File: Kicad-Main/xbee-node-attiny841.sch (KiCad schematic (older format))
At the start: 40 parts, among them P10 CONN_1, P11 CONN_1, P12 CONN_1, P13 CONN_1, P14 CONN_1, P15 CONN_1, P16 CONN_1, P17 CONN_1, P18 CONN_1, P2 XBee Adaptor, P3 Test, P4 Battery, P5 XBee-ext-1, P6 XBee-ext-2, P7 CONN_1, P8 CONN_1, P9 CONN_1, Q2 S9014, Q3 2N7000, U1 ATTINY841, U2 MAX952ESA, U3 TPS77033

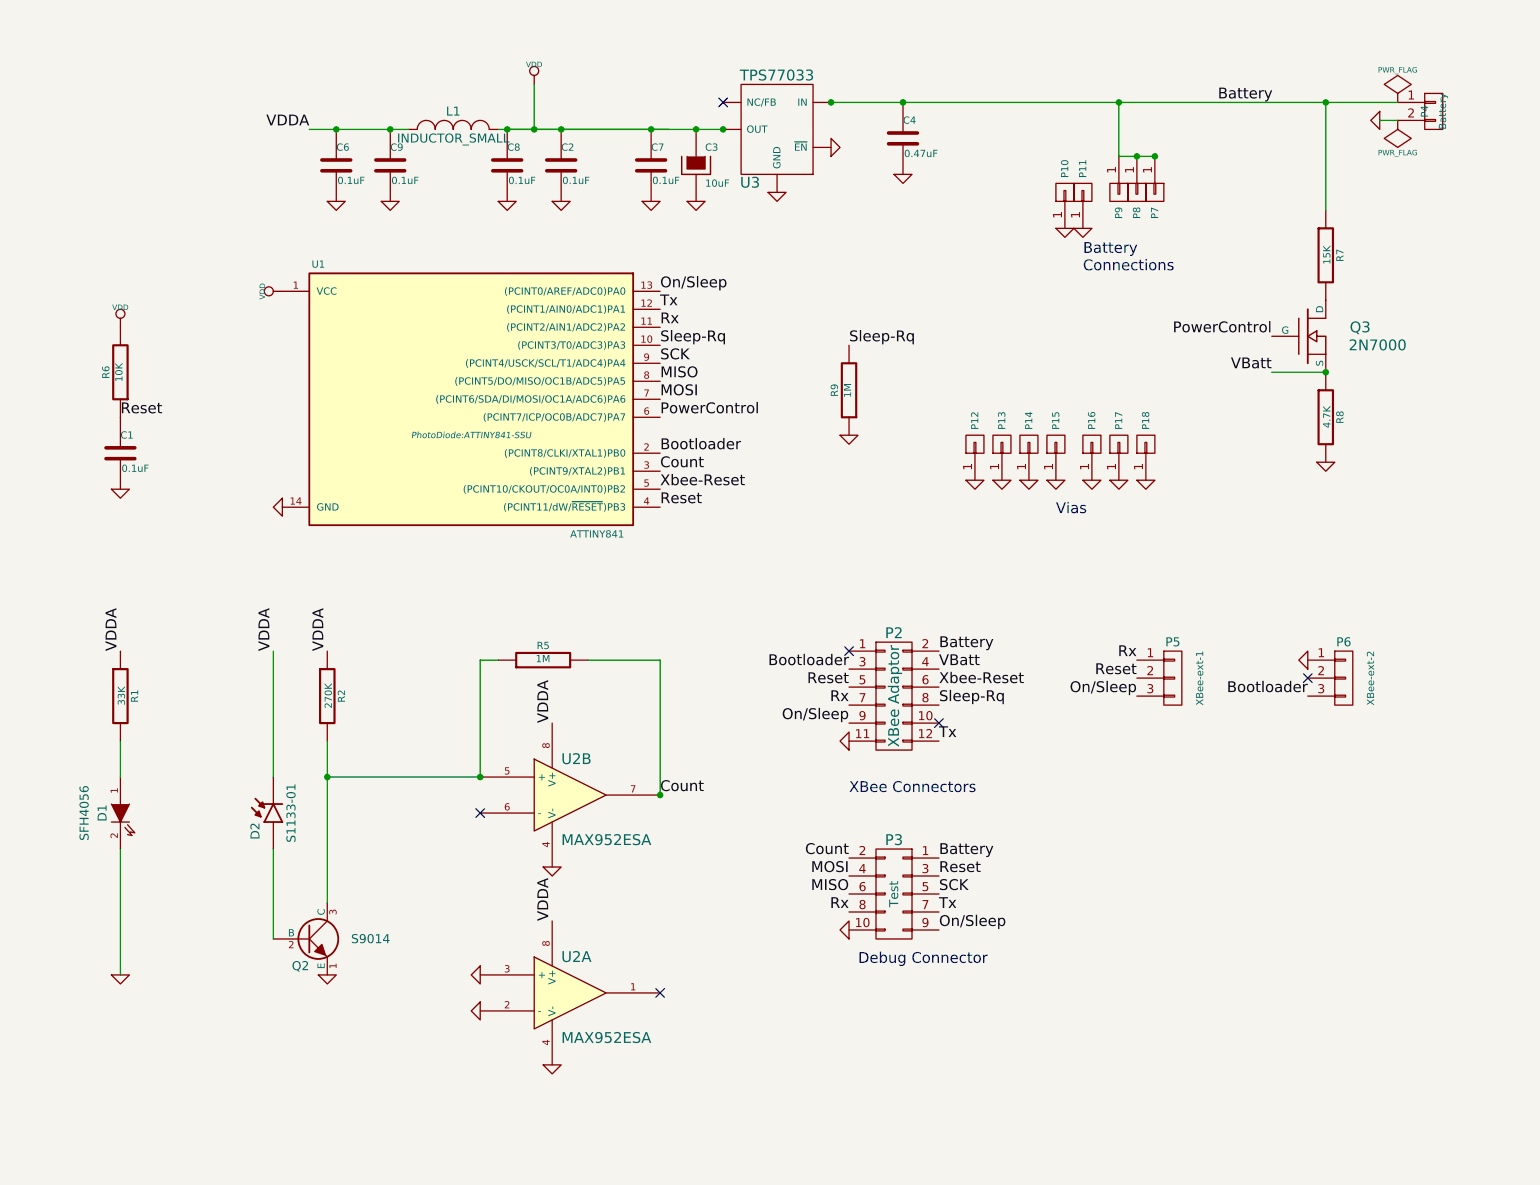
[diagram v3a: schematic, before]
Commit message: Major new version of the PCBs for next stage of production run.
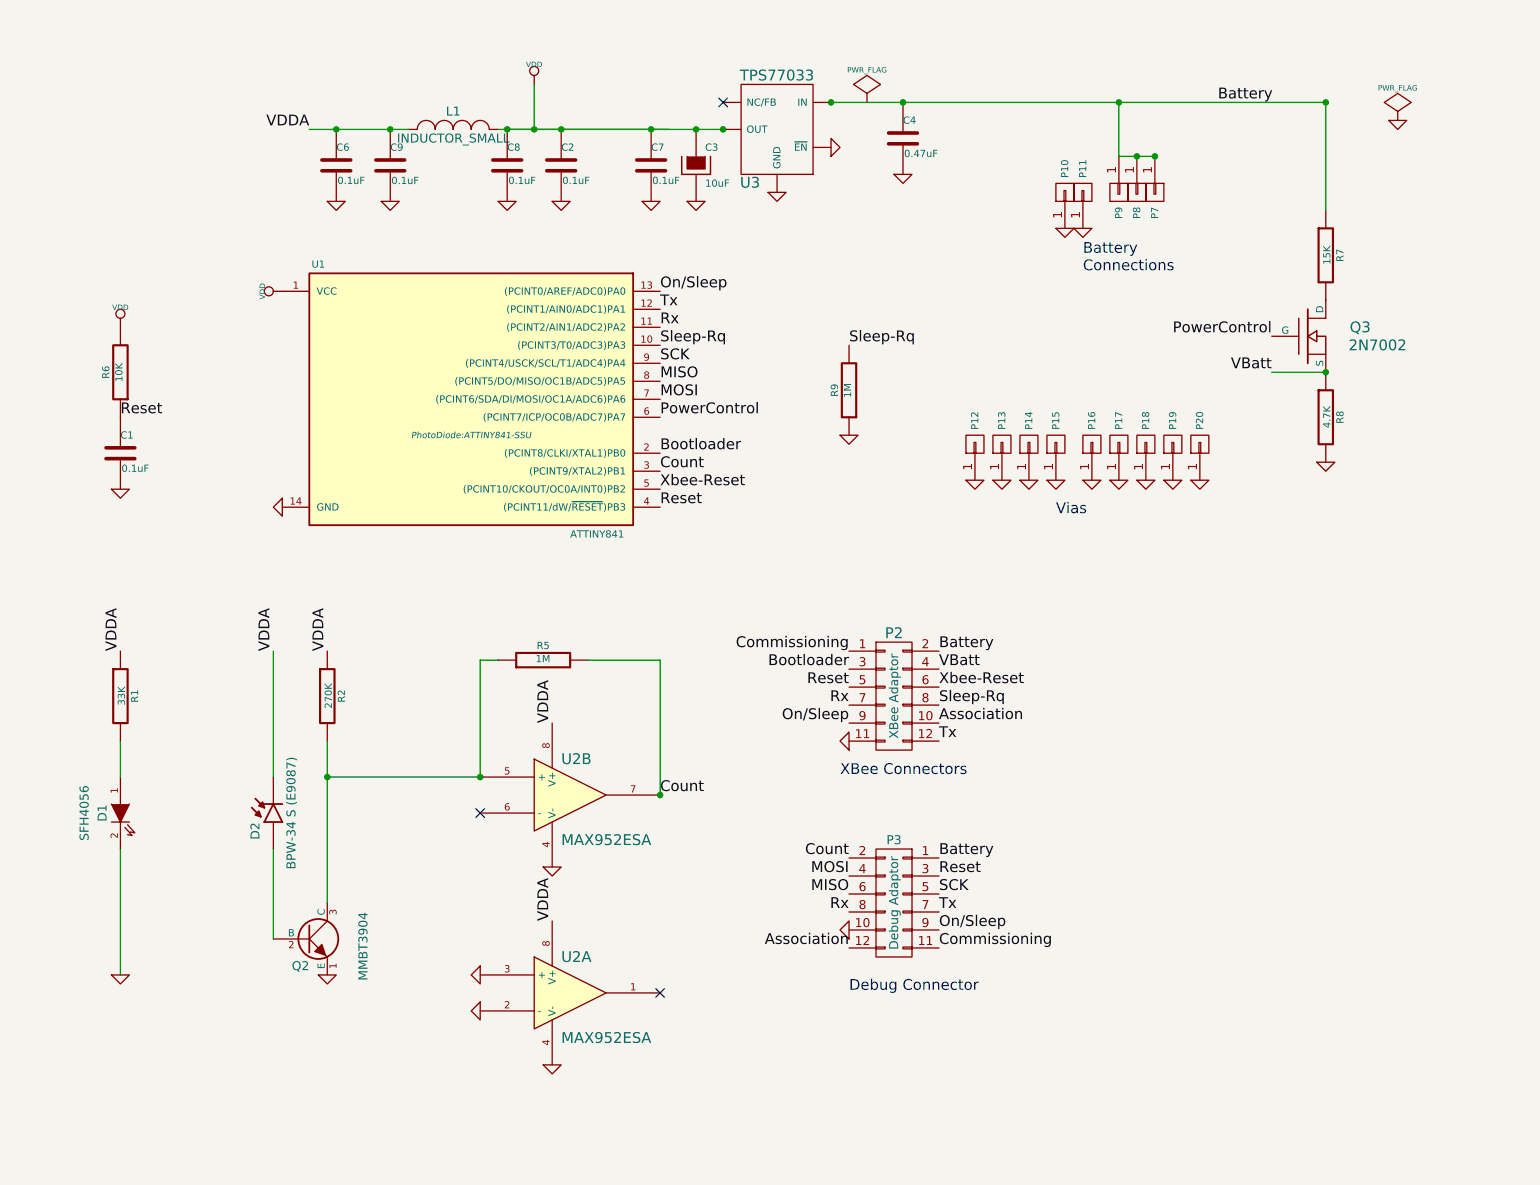
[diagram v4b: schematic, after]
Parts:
- removed P3: Test, PhotoDiode:pin_header_2mm_2x5, symbol CONN_02X05
- removed P4: Battery, PhotoDiode:SIL-2, symbol CONN_01X02
- removed P5: XBee-ext-1, PhotoDiode:pin_header_2mm_1x3, symbol CONN_01X03
- removed P6: XBee-ext-2, PhotoDiode:pin_header_2mm_1x3, symbol CONN_01X03
- added P19, P20: CONN_1, PhotoDiode:THROUGHVIA, symbol CONN_01X01
- added P3: Debug Adaptor, PhotoDiode:pin_smd_header_2mm_2x6, symbol CONN_02X06
- D2: value S1133-01 -> BPW-34 S (E9087); footprint PhotoDiode:S1133TH -> PhotoDiode:BPW34
- L1: footprint PhotoDiode:SM0603_Resistor -> PhotoDiode:R_0805
- Q2: value S9014 -> MMBT3904
- Q3: value 2N7000 -> 2N7002
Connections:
- net labels added: Association, Commissioning
- wire segments 20 -> 19
- no-connect marks 6 -> 3
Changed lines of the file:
@@
 Sheet 1 1
 Title "XBee ATTiny4313 Counting Node"
-Date "26 Jul 2014"
-Rev "0.0"
+Date "08 April 2016"
+Rev "1.0"
 Comp "K. Sarkies"
 Comment1 ""
@@
 $EndDescr
 $Comp
-L CONN_01X02 P4
-U 1 1 53D32A7E
-P 10250 1450
-F 0 "P4" V 10200 1450 40  0000 C CNN
-F 1 "Battery" V 10300 1450 40  0000 C CNN
-F 2 "PhotoDiode:SIL-2" H 10250 1450 60  0001 C CNN
-F 3 "" H 10250 1450 60  0000 C CNN
-	1    10250 1450
-	1    0    0    -1
-$EndComp
-$Comp
 L MOSFET_N-RESCUE-xbee-node-attiny841 Q3
 U 1 1 53D32AE5
 P 9550 2700
 F 0 "Q3" H 9900 2750 60  0000 R CNN
-F 1 "2N7000" H 10100 2650 60  0000 R CNN
+F 1 "2N7002" H 10100 2650 60  0000 R CNN
 F 2 "PhotoDiode:SOT23GDS" H 9550 2700 60  0001 C CNN
 F 3 "" H 9550 2700 60  0000 C CNN
@@
 P 4000 6050
 F 0 "Q2" H 4000 5900 50  0000 R CNN
-F 1 "S9014" H 4450 6050 50  0000 R CNN
+F 1 "MMBT3904" V 4300 6200 50  0000 R CNN
 F 2 "PhotoDiode:SOT23EBC" H 4000 6050 60  0001 C CNN
 F 3 "" H 4000 6050 60  0000 C CNN
@@
 P 7250 4700
 F 0 "P2" H 7250 5050 60  0000 C CNN
-F 1 "XBee Adaptor" V 7250 4700 60  0000 C CNN
+F 1 "XBee Adaptor" V 7250 4700 50  0000 C CNN
 F 2 "PhotoDiode:pin_header_2mm_2x6" H 7250 4700 60  0001 C CNN
 F 3 "" H 7250 4700 60  0000 C CNN
@@
 	1    2950 3350
 	1    0    0    -1
-$EndComp
-$Comp
-L CONN_02X05 P3
-U 1 1 53E0177A
-P 7250 5800
-F 0 "P3" H 7250 6100 60  0000 C CNN
-F 1 "Test" V 7250 5800 50  0000 C CNN
-F 2 "PhotoDiode:pin_header_2mm_2x5" H 7250 5800 60  0001 C CNN
-F 3 "" H 7250 5800 60  0000 C CNN
-	1    7250 5800
-	-1   0    0    -1
 $EndComp
 $Comp
@@
 L PWR_FLAG #FLG016
 U 1 1 53E1FC41
-P 10050 1400
-F 0 "#FLG016" H 10050 1495 30  0001 C CNN
-F 1 "PWR_FLAG" H 10050 1580 30  0000 C CNN
-F 2 "" H 10050 1400 60  0000 C CNN
-F 3 "" H 10050 1400 60  0000 C CNN
-	1    10050 1400
+P 7100 1400
+F 0 "#FLG016" H 7100 1495 30  0001 C CNN
+F 1 "PWR_FLAG" H 7100 1580 30  0000 C CNN
+F 2 "" H 7100 1400 60  0000 C CNN
+F 3 "" H 7100 1400 60  0000 C CNN
+	1    7100 1400
 	1    0    0    -1
 $EndComp
@@
 L GND-RESCUE-xbee-node-attiny841 #PWR021
 U 1 1 53E26458
-P 9950 1500
-F 0 "#PWR021" H 9950 1500 30  0001 C CNN
-F 1 "GND" H 9950 1430 30  0001 C CNN
-F 2 "" H 9950 1500 60  0000 C CNN
-F 3 "" H 9950 1500 60  0000 C CNN
-	1    9950 1500
-	0    1    1    0
+P 10050 1500
+F 0 "#PWR021" H 10050 1500 30  0001 C CNN
+F 1 "GND" H 10050 1430 30  0001 C CNN
+F 2 "" H 10050 1500 60  0000 C CNN
+F 3 "" H 10050 1500 60  0000 C CNN
+	1    10050 1500
+	1    0    0    -1
 $EndComp
 $Comp
@@
 F 3 "" H 10050 1500 60  0000 C CNN
 	1    10050 1500
-	1    0    0    1
+	-1   0    0    -1
 $EndComp
 Text Label 5950 2850 0    60   ~ 0
@@
 Text Label 7000 5700 2    60   ~ 0
 MOSI
-NoConn ~ 7000 4450
-NoConn ~ 7500 4850
 $Comp
 L C-RESCUE-xbee-node-attiny841 C6
@@
 On/Sleep
 $Comp
-L CONN_01X03 P5
-U 1 1 53F2B594
-P 8800 4600
-F 0 "P5" H 8800 4800 50  0000 C CNN
-F 1 "XBee-ext-1" V 8950 4600 40  0000 C CNN
-F 2 "PhotoDiode:pin_header_2mm_1x3" H 8800 4600 60  0001 C CNN
-F 3 "" H 8800 4600 60  0000 C CNN
-	1    8800 4600
-	1    0    0    -1
-$EndComp
-$Comp
-L CONN_01X03 P6
-U 1 1 53F2B605
-P 9750 4600
-F 0 "P6" H 9750 4800 50  0000 C CNN
-F 1 "XBee-ext-2" V 9900 4600 40  0000 C CNN
-F 2 "PhotoDiode:pin_header_2mm_1x3" H 9750 4600 60  0001 C CNN
-F 3 "" H 9750 4600 60  0000 C CNN
-	1    9750 4600
-	1    0    0    -1
-$EndComp
-Text Label 8600 4700 2    60   ~ 0
-On/Sleep
-Text Label 8600 4500 2    60   ~ 0
-Rx
-Text Label 8600 4600 2    60   ~ 0
-Reset
-Text Label 9550 4700 2    60   ~ 0
-Bootloader
-NoConn ~ 9550 4600
-$Comp
 L CONN_01X01 P7
 U 1 1 53F2CFA4
@@
 	1    0    0    -1
 $EndComp
-$Comp
-L GND-RESCUE-xbee-node-attiny841 #PWR034
-U 1 1 53FEF658
-P 9550 4500
-F 0 "#PWR034" H 9550 4500 30  0001 C CNN
-F 1 "GND" H 9550 4430 30  0001 C CNN
-F 2 "" H 9550 4500 60  0000 C CNN
-F 3 "" H 9550 4500 60  0000 C CNN
-	1    9550 4500
-	0    1    -1   0
-$EndComp
 Text Label 9050 1400 0    60   ~ 0
 Battery
@@
 P 3800 5350
 F 0 "D2" H 3700 5450 50  0000 C CNN
-F 1 "S1133-01" H 3800 5250 50  0000 C CNN
-F 2 "PhotoDiode:S1133TH" H 3800 5350 60  0001 C CNN
+F 1 "BPW-34 S (E9087)" H 3800 5250 50  0000 C CNN
+F 2 "PhotoDiode:BPW34" H 3800 5350 60  0001 C CNN
 F 3 "" H 3800 5350 60  0000 C CNN
 	1    3800 5350
@@
 $EndComp
 $Comp
-L GND-RESCUE-xbee-node-attiny841 #PWR035
+L GND-RESCUE-xbee-node-attiny841 #PWR034
 U 1 1 5482395B
 P 7000 3250
-F 0 "#PWR035" H 7000 3250 30  0001 C CNN
+F 0 "#PWR034" H 7000 3250 30  0001 C CNN
 F 1 "GND" H 7000 3180 30  0001 C CNN
 F 2 "" H 7000 3250 60  0000 C CNN
@@
 F 0 "L1" H 4800 1650 50  0000 C CNN
 F 1 "INDUCTOR_SMALL" H 4800 1500 50  0000 C CNN
-F 2 "PhotoDiode:SM0603_Resistor" H 4800 1550 60  0001 C CNN
+F 2 "PhotoDiode:R_0805" H 4800 1550 60  0001 C CNN
 F 3 "" H 4800 1550 60  0000 C CNN
 	1    4800 1550
@@
 $EndComp
 $Comp
-L GND-RESCUE-xbee-node-attiny841 #PWR036
+L GND-RESCUE-xbee-node-attiny841 #PWR035
 U 1 1 548D0F71
 P 5100 1950
-F 0 "#PWR036" H 5100 1950 30  0001 C CNN
+F 0 "#PWR035" H 5100 1950 30  0001 C CNN
 F 1 "GND" H 5100 1880 30  0001 C CNN
 F 2 "" H 5100 1950 60  0000 C CNN
@@
 $EndComp
 $Comp
-L GND-RESCUE-xbee-node-attiny841 #PWR037
+L GND-RESCUE-xbee-node-attiny841 #PWR036
 U 1 1 548D117F
 P 4450 1950
-F 0 "#PWR037" H 4450 1950 30  0001 C CNN
+F 0 "#PWR036" H 4450 1950 30  0001 C CNN
 F 1 "GND" H 4450 1880 30  0001 C CNN
 F 2 "" H 4450 1950 60  0000 C CNN
@@
 	5950 5250 5950 4500
 Wire Wire Line
-	6900 1400 10050 1400
+	6900 1400 9650 1400
 Wire Wire Line
 	9650 1400 9650 2000
@@
 Connection ~ 8700 1700
 Connection ~ 8600 1700
-Wire Wire Line
-	10050 1500 9950 1500
 Wire Wire Line
 	5050 1550 6300 1550
@@
 Text Notes 8150 3700 0    60   ~ 0
 Vias
-Text Notes 7000 5250 0    60   ~ 0
+Text Notes 6950 5150 0    60   ~ 0
 XBee Connectors
-Text Notes 7050 6200 0    60   ~ 0
+Text Notes 7000 6350 0    60   ~ 0
 Debug Connector
+Text Label 7000 4450 2    60   ~ 0
+Commissioning
+Text Label 7500 4850 0    60   ~ 0
+Association
+$Comp
+L CONN_02X06 P3
+U 1 1 570748A7
+P 7250 5850
+F 0 "P3" H 7250 6200 50  0000 C CNN
+F 1 "Debug Adaptor" V 7250 5850 50  0000 C CNN
+F 2 "PhotoDiode:pin_smd_header_2mm_2x6" H 7250 4650 50  0001 C CNN
+F 3 "" H 7250 4650 50  0000 C CNN
+	1    7250 5850
+	-1   0    0    -1
+$EndComp
+Text Label 7000 6100 2    60   ~ 0
+Association
+Text Label 7500 6100 0    60   ~ 0
+Commissioning
+$Comp
+L CONN_01X01 P19
+U 1 1 57079BA8
+P 8800 3300
+F 0 "P19" H 8880 3300 40  0000 L CNN
+F 1 "CONN_1" H 8800 3355 30  0001 C CNN
+F 2 "PhotoDiode:THROUGHVIA" H 8800 3300 60  0001 C CNN
+F 3 "" H 8800 3300 60  0000 C CNN
+	1    8800 3300
+	0    -1   -1   0
+$EndComp
+$Comp
+L GND-RESCUE-xbee-node-attiny841 #PWR037
+U 1 1 57079D2F
+P 8800 3500
+F 0 "#PWR037" H 8800 3500 30  0001 C CNN
+F 1 "GND" H 8800 3430 30  0001 C CNN
+F 2 "" H 8800 3500 60  0000 C CNN
+F 3 "" H 8800 3500 60  0000 C CNN
+	1    8800 3500
+	1    0    0    -1
+$EndComp
+$Comp
+L CONN_01X01 P20
+U 1 1 5707A0C5
+P 8950 3300
+F 0 "P20" H 9030 3300 40  0000 L CNN
+F 1 "CONN_1" H 8950 3355 30  0001 C CNN
+F 2 "PhotoDiode:THROUGHVIA" H 8950 3300 60  0001 C CNN
+F 3 "" H 8950 3300 60  0000 C CNN
+	1    8950 3300
+	0    -1   -1   0
+$EndComp
+$Comp
+L GND-RESCUE-xbee-node-attiny841 #PWR038
+U 1 1 5707A217
+P 8950 3500
+F 0 "#PWR038" H 8950 3500 30  0001 C CNN
+F 1 "GND" H 8950 3430 30  0001 C CNN
+F 2 "" H 8950 3500 60  0000 C CNN
+F 3 "" H 8950 3500 60  0000 C CNN
+	1    8950 3500
+	1    0    0    -1
+$EndComp
 $EndSCHEMATC

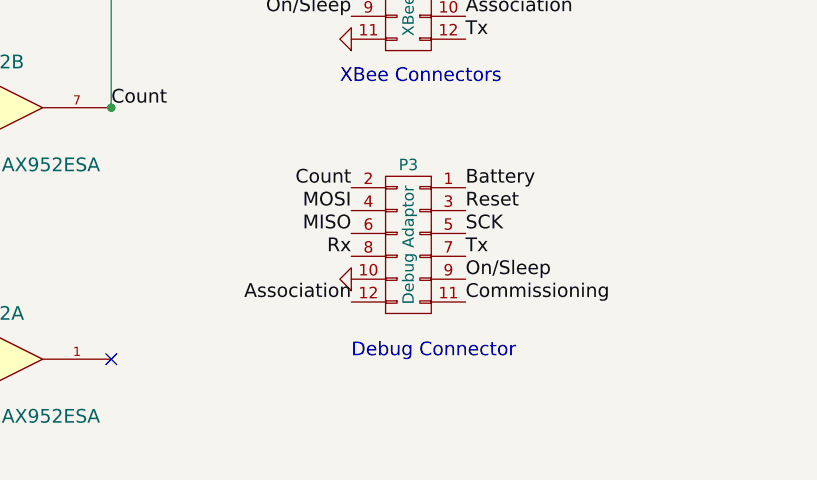
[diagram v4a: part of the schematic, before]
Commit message: Main PCB. Changes to debug connector to bring out XBee association and commissioning signals. Change photodiode to BPW34. Minor change to battery mount to increase drill hole and move holes to spec. The LED mount footprint has also been changed to match the power and ground on the mounting board itself.
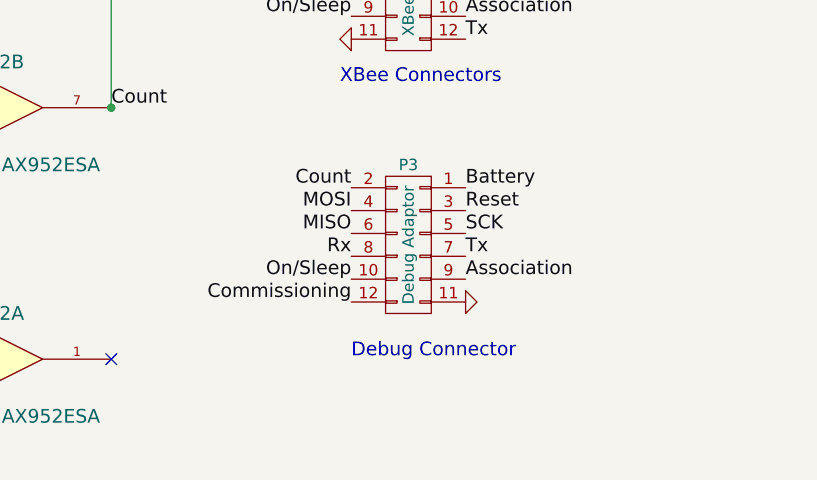
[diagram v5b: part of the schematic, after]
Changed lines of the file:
@@
 L GND-RESCUE-xbee-node-attiny841 #PWR015
 U 1 1 53E0741A
-P 7000 6000
-F 0 "#PWR015" H 7000 6000 30  0001 C CNN
-F 1 "GND" H 7000 5930 30  0001 C CNN
-F 2 "" H 7000 6000 60  0000 C CNN
-F 3 "" H 7000 6000 60  0000 C CNN
-	1    7000 6000
-	0    1    -1   0
+P 7500 6100
+F 0 "#PWR015" H 7500 6100 30  0001 C CNN
+F 1 "GND" H 7500 6030 30  0001 C CNN
+F 2 "" H 7500 6100 60  0000 C CNN
+F 3 "" H 7500 6100 60  0000 C CNN
+	1    7500 6100
+	0    -1   -1   0
 $EndComp
 NoConn ~ 6300 1400
@@
 Text Label 7000 4550 2    60   ~ 0
 Bootloader
-Text Label 7500 6000 0    60   ~ 0
+Text Label 7000 6000 2    60   ~ 0
 On/Sleep
 $Comp
@@
 	-1   0    0    -1
 $EndComp
+Text Label 7500 6000 0    60   ~ 0
+Association
 Text Label 7000 6100 2    60   ~ 0
-Association
-Text Label 7500 6100 0    60   ~ 0
 Commissioning
 $Comp
